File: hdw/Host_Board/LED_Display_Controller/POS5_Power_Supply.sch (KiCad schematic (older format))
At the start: 0 parts

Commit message: revised part numbers in BOM
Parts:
- added C? (x3): C, symbol LED_Display_Local_Library:C_Custom
- added C?: 2.2uF, symbol LED_Display_Local_Library:C_Custom
- added C? (x2): 0.1uF, symbol LED_Display_Local_Library:C_Custom
- added L?: L_Custom, symbol LED_Display_Local_Library:L_Custom
- added R? (x2): R, symbol Custom_Library:R_Custom
- added R? (x4): 10k, symbol Custom_Library:R_Custom
- added U?: LTC3624DD, Housings_DFN_QFN:DFN-8-1EP_3x3mm_Pitch0.5mm, symbol LED_Display_Local_Library:LTC3624DD
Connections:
- new net: L?.1, U?.1 (SW)
- new net: C?.2, R?.1, R?.2, U?.5 (FB)
- new net: C?.1, R?.1, U?.6 (INTVCC)
- new net: R?.1, R?.2, U?.7 (MODE/SYNC)
- new net +12V: C?.1, C?.1, U?.2 (VIN)
- new net +3V3: R?.1
- new net +5V: C?.1, C?.1, C?.1, L?.2, R?.1
- new net GND: C?.2, C?.2, C?.2, C?.2, C?.2, R?.2, R?.2, R?.2, U?.8 (GND), U?.9 (GND)
- new net POS5_PGOOD: R?.2, U?.4 (PGOOD)
- new net POS5_RUN: R?.1, U?.3 (RUN)

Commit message: Added a few pages and edits
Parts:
- removed C? (x2): C, symbol LED_Display_Local_Library:C_Custom
- removed R?: R, symbol Custom_Library:R_Custom
- added C? (x3): 22uF, symbol LED_Display_Local_Library:C_Custom
- added R?: 13.7k, symbol Custom_Library:R_Custom
- C?: value C -> 33pF; Dielectric Er -> NP0; Voltage V -> 50V; display_footprint Foot -> 0603
- C?: Dielectric Er -> X5R; Voltage 10V -> 16V; display_footprint Foot -> 0805
- L?: value L_Custom -> 3.3uH; Ampacity A -> 2.7A; Tolerance Tol -> 20%; display_footprint Foot -> IHLP1212
- R?: value R -> 100k; Tolerance Tol -> 1%; Wattage W -> 1/10W; display_footprint Foot -> 0603
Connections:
- net +12V: now also C?.1
- net +5V: now also C?.1, C?.1
- net GND: now also C?.2, C?.2, C?.2, R?.2
- net at C?.2, R?.2, U?.5 (FB): now also R?.1
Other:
- moved on the sheet: C?, L?, R?, U?

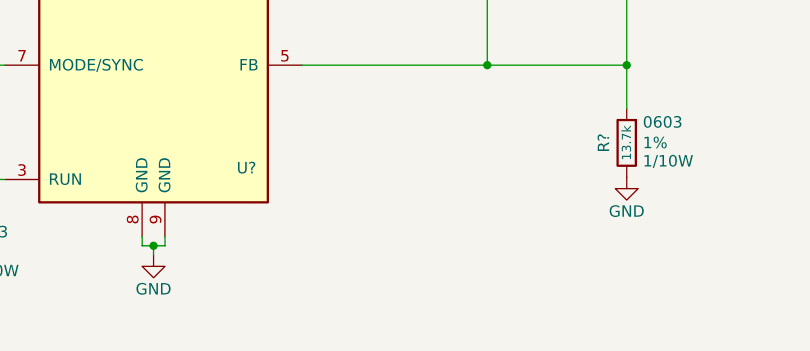
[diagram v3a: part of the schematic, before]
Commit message: Added graphical symbols to certain sheets
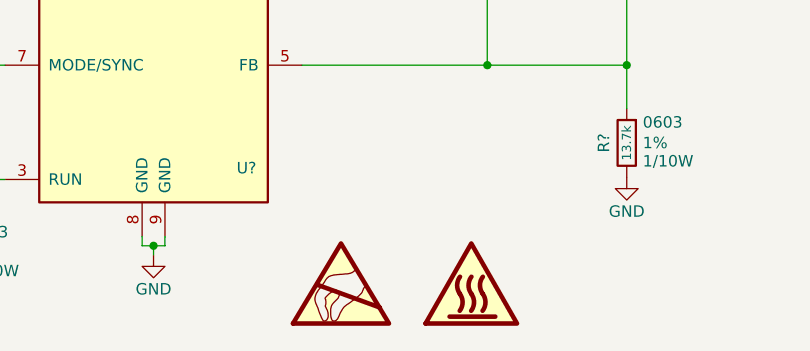
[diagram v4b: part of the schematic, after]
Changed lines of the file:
@@
 	9090 3150 9090 3230
 Connection ~ 9090 3230
+$Comp
+L Graphic:SYM_ESD_Large #SYM?
+U 1 1 5C050F30
+P 5760 5160
+AR Path="/5BAAE0FA/5C050F30" Ref="#SYM?"  Part="1"
+AR Path="/5BB182B1/5C050F30" Ref="#SYM?"  Part="1"
+AR Path="/5BE5222A/5C050F30" Ref="#SYM?"  Part="1"
+F 0 "#SYM?" H 5760 5360 50  0001 C CNN
+F 1 "SYM_ESD_Large" H 5760 4910 50  0001 C CNN
+F 2 "" H 5755 5130 50  0001 C CNN
+F 3 "~" H 5755 5130 50  0001 C CNN
+	1    5760 5160
+	1    0    0    -1
+$EndComp
+$Comp
+L Graphic:SYM_Hot_Large #SYM?
+U 1 1 5C064EC3
+P 6330 5160
+F 0 "#SYM?" H 6330 5360 50  0001 C CNN
+F 1 "SYM_Hot_Large" H 6330 4910 50  0001 C CNN
+F 2 "" H 6330 4960 50  0001 C CNN
+F 3 "~" H 6360 4960 50  0001 C CNN
+	1    6330 5160
+	1    0    0    -1
+$EndComp
 $EndSCHEMATC

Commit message: Cleaned up a few sheets
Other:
- note added: "Designed for 2A Max Iout"
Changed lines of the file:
@@
 	1    0    0    -1
 $EndComp
+Text Notes 8240 4260 0    50   ~ 0
+Designed for 2A Max Iout
 $EndSCHEMATC

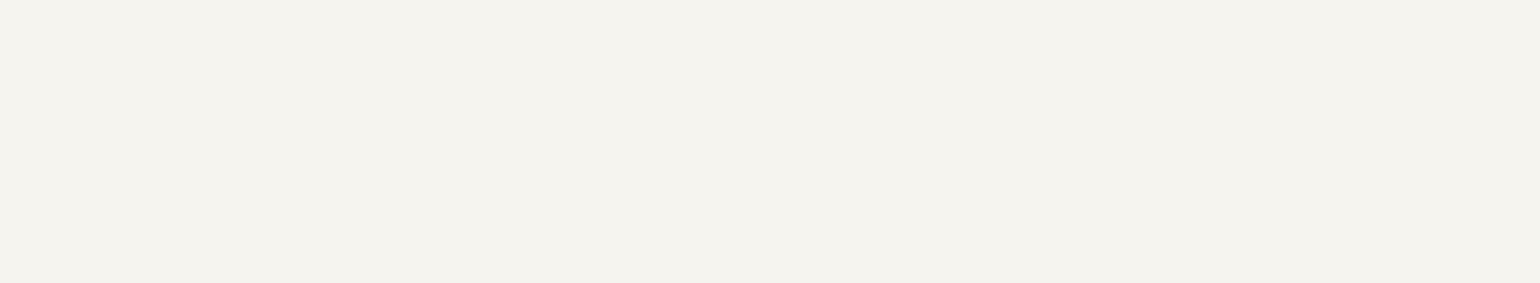
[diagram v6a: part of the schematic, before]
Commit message: Added titles and MU logo to each sheet
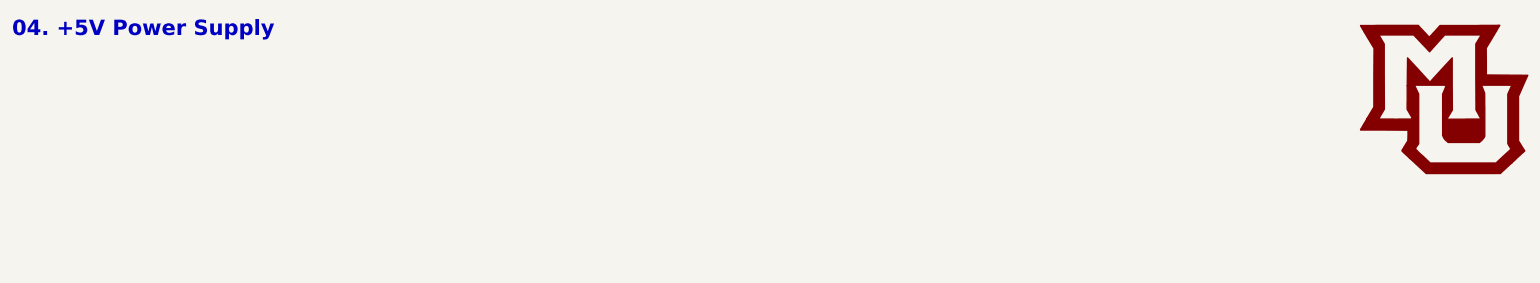
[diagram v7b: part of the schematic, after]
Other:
- note added: "04. +5V Power Supply"
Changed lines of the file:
@@
 Text Notes 8240 4260 0    50   ~ 0
 Designed for 2A Max Iout
+Text Notes 550  700  0    100  ~ 20
+04. +5V Power Supply
+$Comp
+L LED_Display_Local_Library:MU_Logo #G?
+U 1 1 5BFF2E6E
+P 9900 1100
+F 0 "#G?" H 9900 614 60  0001 C CNN
+F 1 "MU_Logo" H 9900 1586 60  0001 C CNN
+F 2 "" H 9900 1100 50  0001 C CNN
+F 3 "" H 9900 1100 50  0001 C CNN
+	1    9900 1100
+	1    0    0    -1
+$EndComp
 $EndSCHEMATC
